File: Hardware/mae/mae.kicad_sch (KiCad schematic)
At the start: 1 part, among them Q1 Q_NJFET_DSG

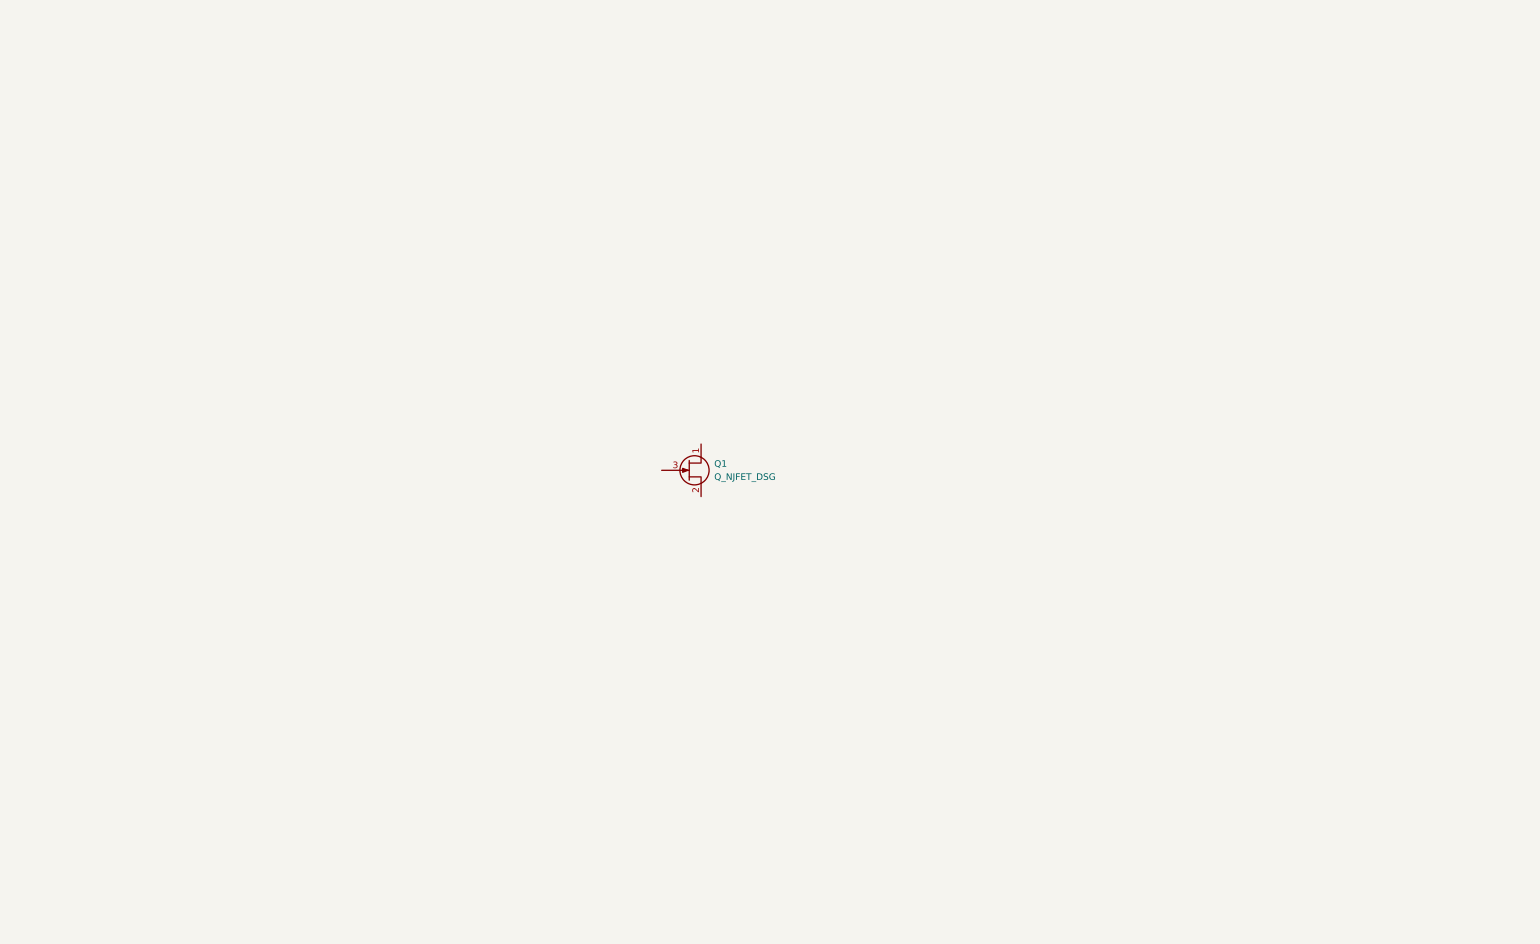
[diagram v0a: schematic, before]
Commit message: Mae rev 1 schems done! power supply and audio out
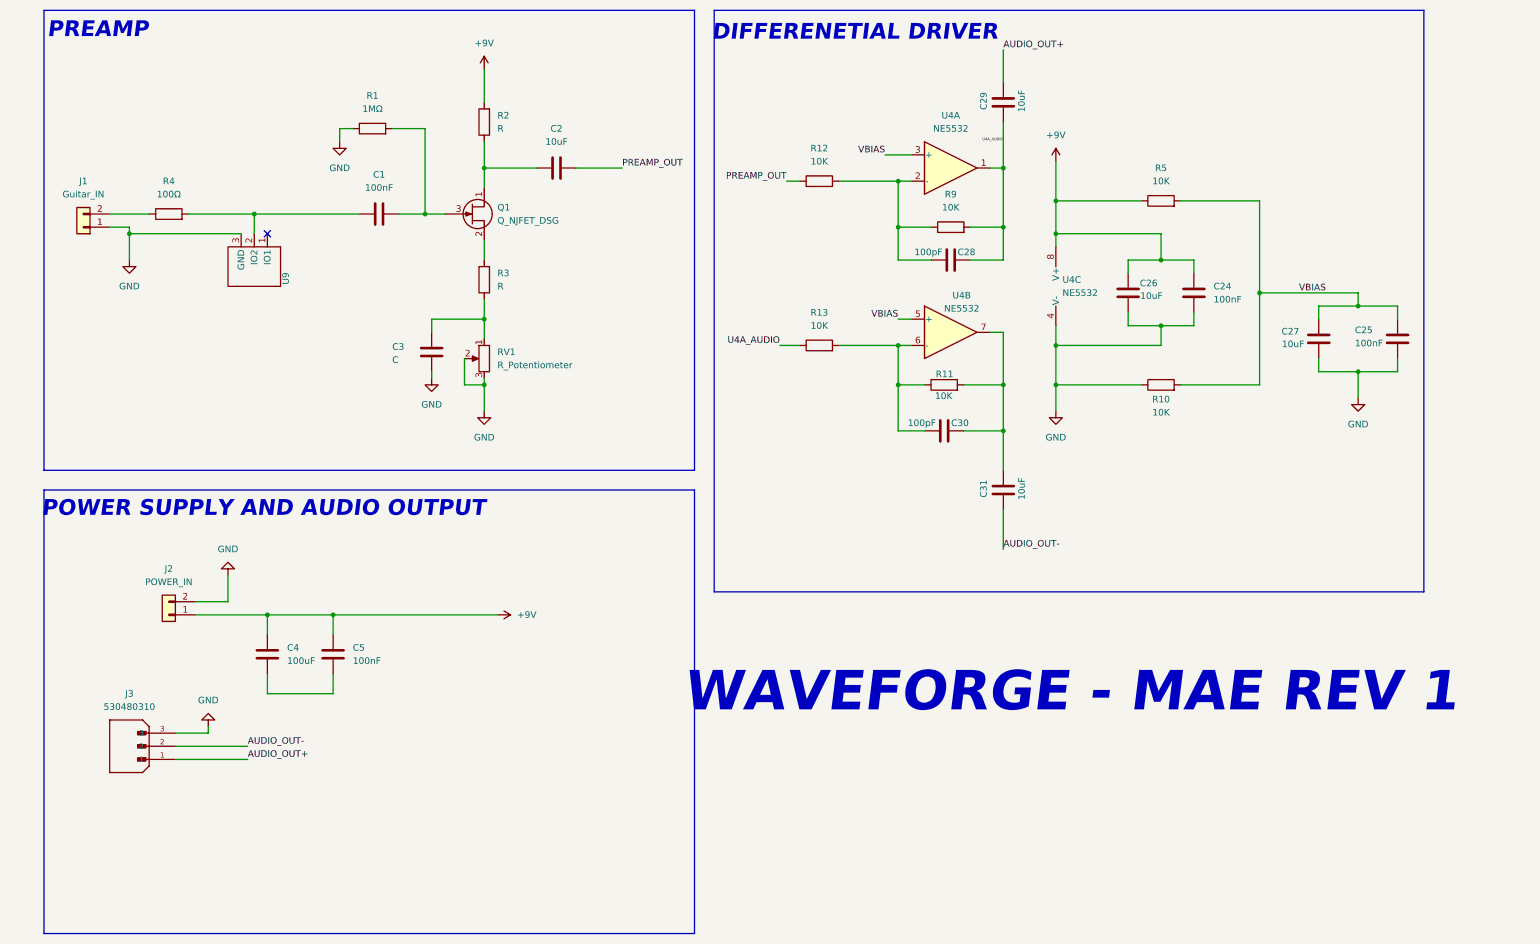
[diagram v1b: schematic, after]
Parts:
- added C1, C5: 100nF, symbol Device:C
- added C2: 10uF, symbol Device:C
- added C24, C25: 100nF, Capacitor_SMD:C_0402_1005Metric_Pad0.74x0.62mm_HandSolder, symbol Device:C
- added C26, C27: 10uF, Capacitor_SMD:C_0402_1005Metric_Pad0.74x0.62mm_HandSolder, symbol Device:C
- added C28, C30: 100pF, Capacitor_SMD:C_0402_1005Metric_Pad0.74x0.62mm_HandSolder, symbol Device:C
- added C29, C31: 10uF, Capacitor_SMD:C_0603_1608Metric_Pad1.08x0.95mm_HandSolder, symbol Device:C
- added C3: C, symbol Device:C
- added C4: 100uF, symbol Device:C
- added J1: Guitar_IN, Connector_JST:JST_PH_S2B-PH-K_1x02_P2.00mm_Horizontal, symbol Connector_Generic:Conn_01x02
- added J2: POWER_IN, Connector_JST:JST_PH_S2B-PH-K_1x02_P2.00mm_Horizontal, symbol Connector_Generic:Conn_01x02
- added J3: 530480310, My Footprints:MOLEX_530480310, symbol My Symbols:530480310
- added R1: 1MΩ, symbol Device:R
- added R10, R11, R12, R13, R5, R9: 10K, Resistor_SMD:R_0402_1005Metric_Pad0.72x0.64mm_HandSolder, symbol Device:R
- added R2, R3: R, symbol Device:R
- added R4: 100Ω, symbol Device:R
- added RV1: R_Potentiometer, symbol Device:R_Potentiometer
- added U4: NE5532, Package_SO:SOIC-8_3.9x4.9mm_P1.27mm, symbol Amplifier_Operational:NE5532
- added U9: (no value), Package_TO_SOT_SMD:SOT-23-3, symbol MyCrystal:ESDS452DBZRQ1
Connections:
- net at Q1.1 (D): now also C2.1, R2.1
- net at Q1.2 (S): now also R3.2
- net at Q1.3 (G): now also C1.2, R1.2
- new net: C28.1, R12.2, R9.1, U4.2 (-)
- new net: C3.2, R3.1, RV1.1
- new net: J1.2 (Pin_2), R4.1
- new net: C1.1, R4.2, U9.2 (IO2)
- new net: C30.1, R11.1, R13.2, U4.6 (-)
- new net: C30.2, C31.2, R11.2, U4.7
- new net: C4.2, C5.2
- new net +9V: C24.1, C26.1, C4.1, C5.1, J2.1 (Pin_1), R2.2, R5.1, U4.8 (V+)
- new net AUDIO_OUT+: C29.2, J3.1
- new net AUDIO_OUT-: C31.1, J3.2
- new net GND: C24.2, C25.2, C26.2, C27.2, C3.1, J1.1 (Pin_1), J2.2 (Pin_2), J3.3, R1.1, R10.1, RV1.2, RV1.3, U4.4 (V-), U9.3 (GND)
- new net PREAMP_OUT: C2.2, R12.1
- new net U4A_AUDIO: C28.2, C29.1, R13.1, R9.2, U4.1
- new net VBIAS: C25.1, C27.1, R10.2, R5.2, U4.3 (+), U4.5 (+)
- no-connect marks 0 -> 1
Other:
- note added: "DIFFERENETIAL DRIVER"
- note added: "POWER SUPPLY AND AUDIO OUTPUT"
- note added: "PREAMP"
- note added: "WAVEFORGE - MAE REV 1"
- moved on the sheet: Q1

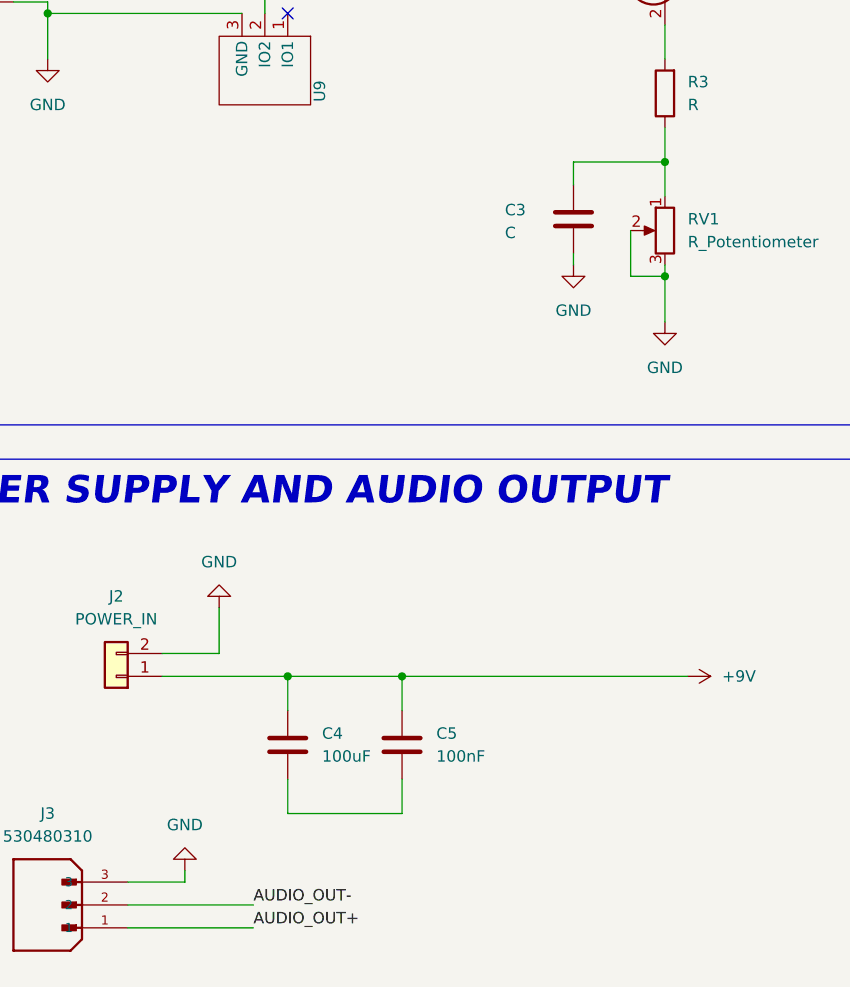
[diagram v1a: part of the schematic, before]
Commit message: Mae footprints assigned, all through hole
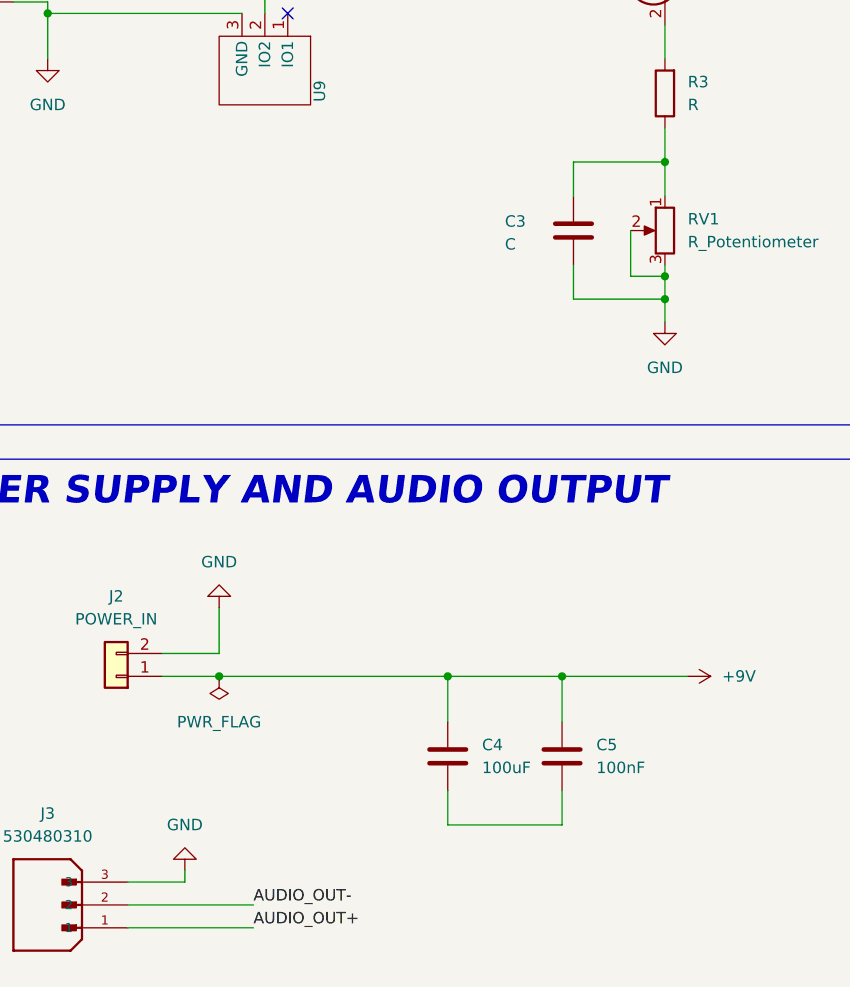
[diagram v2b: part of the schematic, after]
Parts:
- C1, C3, C5: footprint (none) -> Capacitor_THT:C_Disc_D3.0mm_W1.6mm_P2.50mm
- C2: footprint (none) -> Capacitor_THT:C_Radial_D5.0mm_H5.0mm_P2.00mm
- C24, C25, C28, C30: footprint Capacitor_SMD:C_0402_1005Metric_Pad0.74x0.62mm_HandSolder -> Capacitor_THT:C_Disc_D3.0mm_W1.6mm_P2.50mm
- C4: footprint (none) -> Capacitor_THT:C_Radial_D6.3mm_H7.0mm_P2.50mm
- Q1: footprint (none) -> Package_TO_SOT_THT:TO-92_Inline
- R1, R2, R3, R4: footprint (none) -> Resistor_THT:R_Axial_DIN0207
- RV1: footprint (none) -> Connector_JST:JST_PH_S2B-PH-K_1x02_P2.00mm_Horizontal
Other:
- moved on the sheet: C3, C4, C5

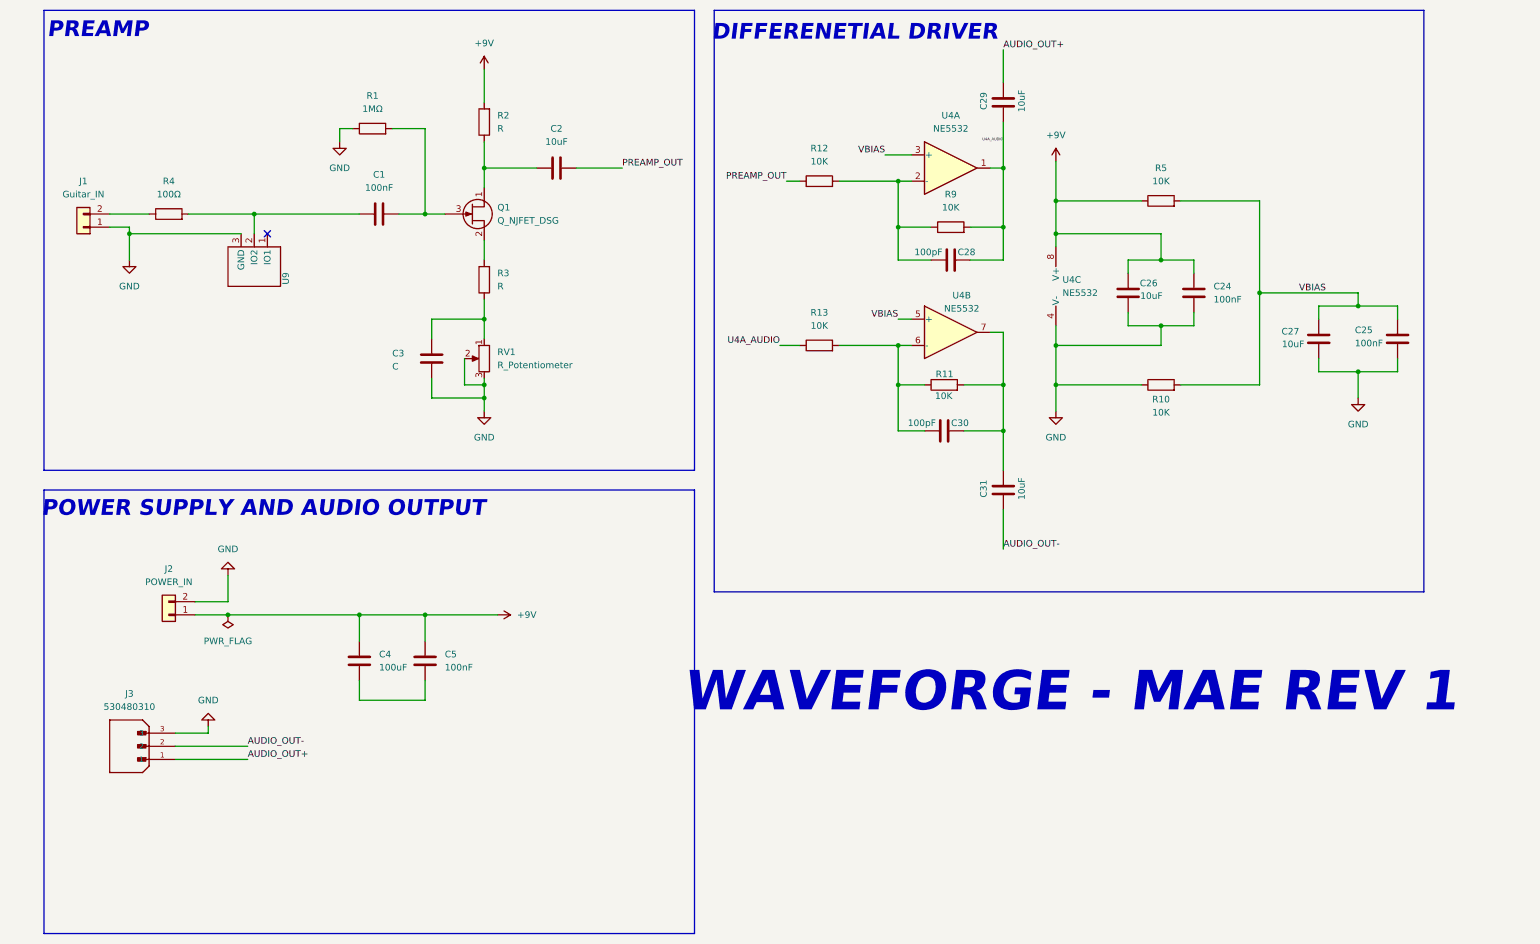
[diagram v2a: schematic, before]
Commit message: Mae layout and routing complete rev 1
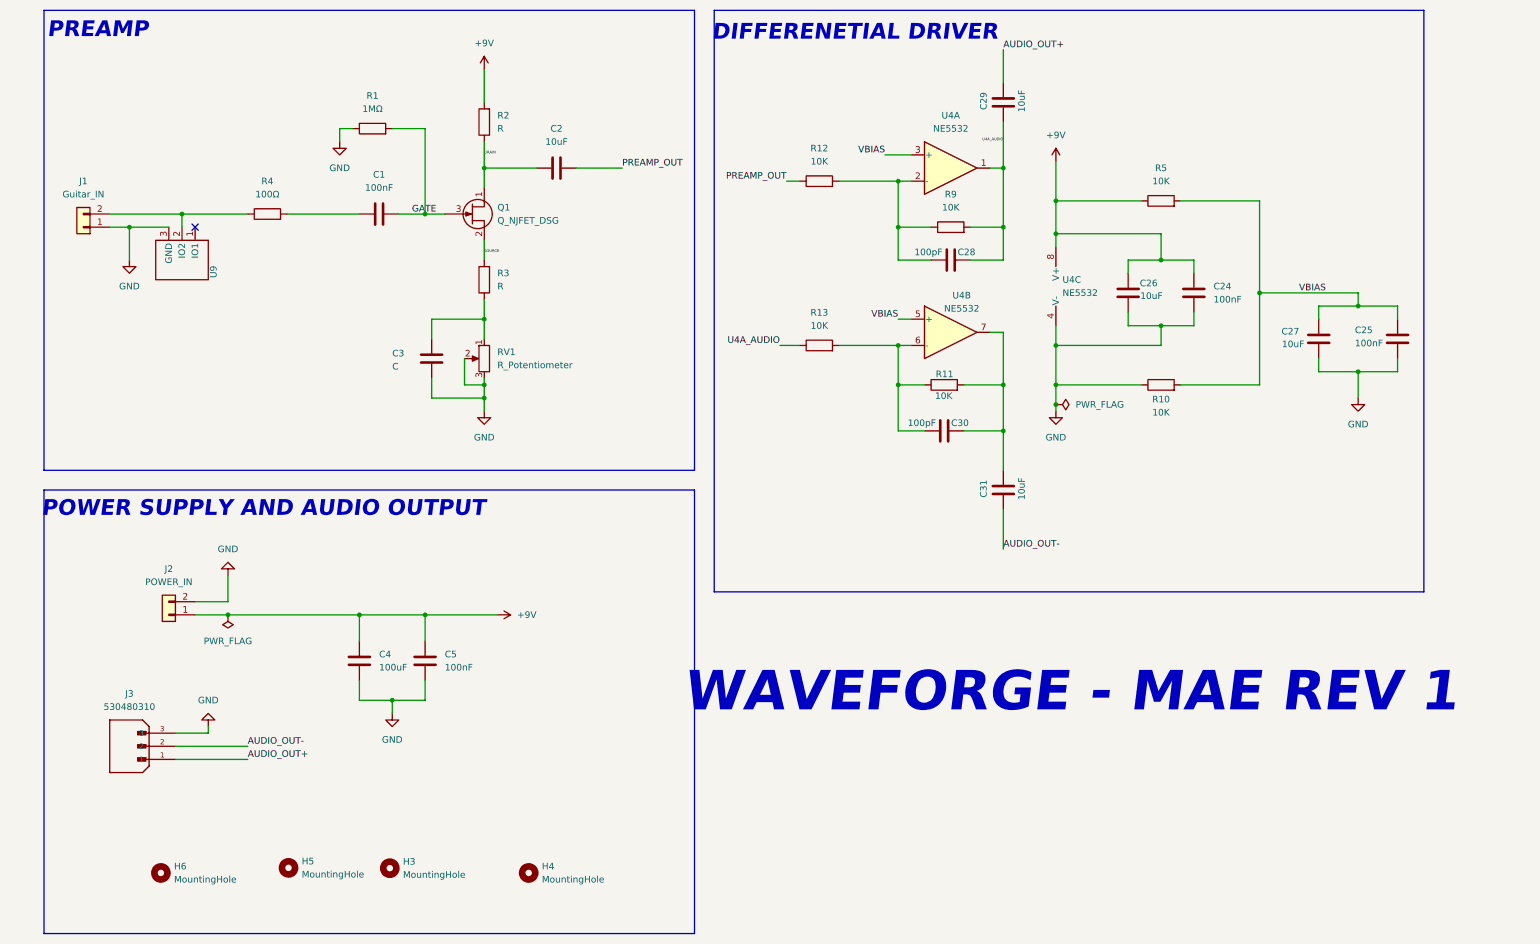
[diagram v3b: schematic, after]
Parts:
- added H3, H4, H5, H6: MountingHole, MountingHole:MountingHole_3.5mm, symbol Mechanical:MountingHole
- C26, C27: footprint Capacitor_SMD:C_0402_1005Metric_Pad0.74x0.62mm_HandSolder -> Capacitor_THT:C_Radial_D5.0mm_H5.0mm_P2.00mm
- C29, C31: footprint Capacitor_SMD:C_0603_1608Metric_Pad1.08x0.95mm_HandSolder -> Capacitor_THT:C_Radial_D5.0mm_H5.0mm_P2.00mm
- C3: footprint Capacitor_THT:C_Disc_D3.0mm_W1.6mm_P2.50mm -> Capacitor_THT:C_Radial_D6.3mm_H7.0mm_P2.50mm
- R1, R2, R3, R4: footprint Resistor_THT:R_Axial_DIN0207 -> Resistor_THT:R_Axial_DIN0207_L6.3mm_D2.5mm_P7.62mm_Horizontal
- R10, R11, R12, R13, R5, R9: footprint Resistor_SMD:R_0402_1005Metric_Pad0.72x0.64mm_HandSolder -> Resistor_THT:R_Axial_DIN0207_L6.3mm_D2.5mm_P7.62mm_Horizontal
- U4: footprint Package_SO:SOIC-8_3.9x4.9mm_P1.27mm -> Package_DIP:DIP-8_W7.62mm
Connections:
- net GND: now also C4.2, C5.2
- net DRAIN: now reaches C2.1, Q1.1 (D), R2.1
- net SOURCE: now reaches Q1.2 (S), R3.2
- net GATE: now reaches C1.2, Q1.3 (G), R1.2
- net at J1.2 (Pin_2), R4.1: now also U9.2 (IO2)
- net at C1.1, R4.2: no longer U9.2 (IO2)
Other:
- moved on the sheet: R4, U9
